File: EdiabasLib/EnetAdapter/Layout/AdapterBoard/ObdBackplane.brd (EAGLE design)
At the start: 36 x 20 mm, 11 parts, among them J1 OBDII, U1 FPC-FFC-CONNECTOR-08-1MM, U2 FPC-FFC-CONNECTOR-08-1MM-L

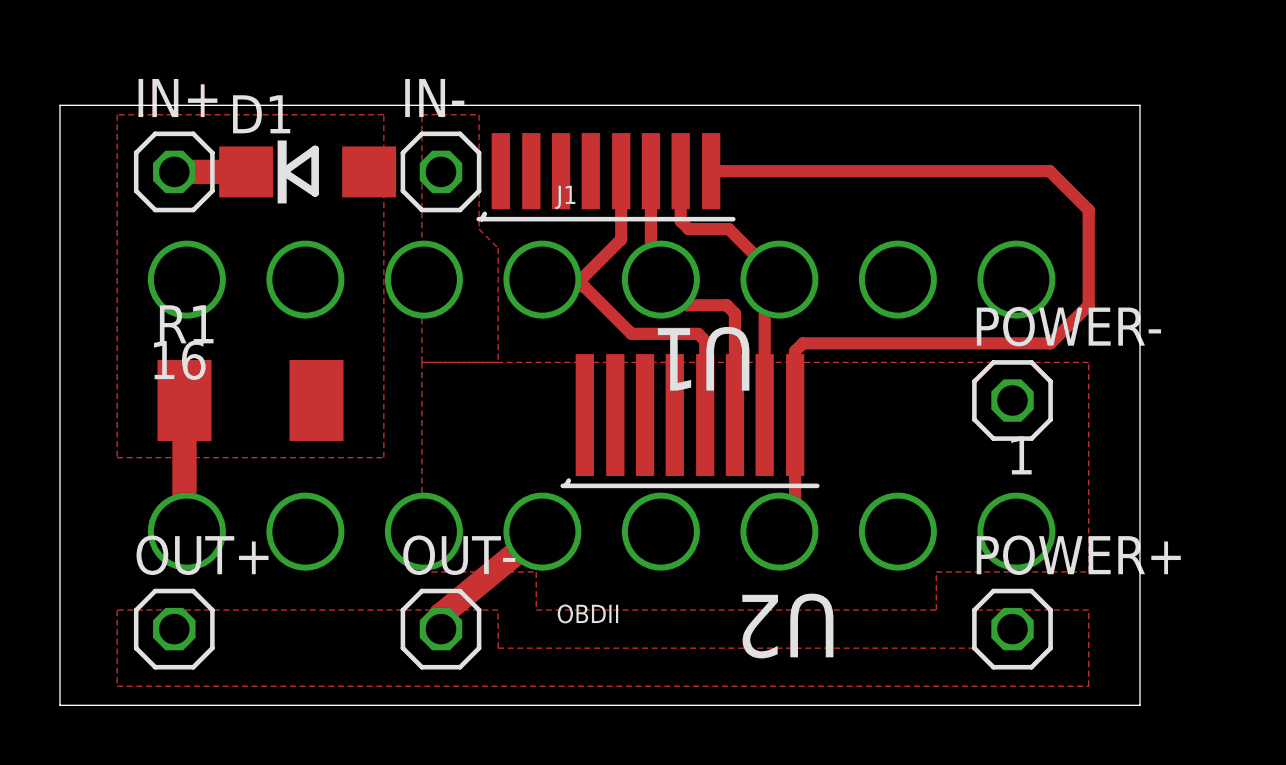
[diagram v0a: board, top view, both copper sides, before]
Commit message: Using larger resistor
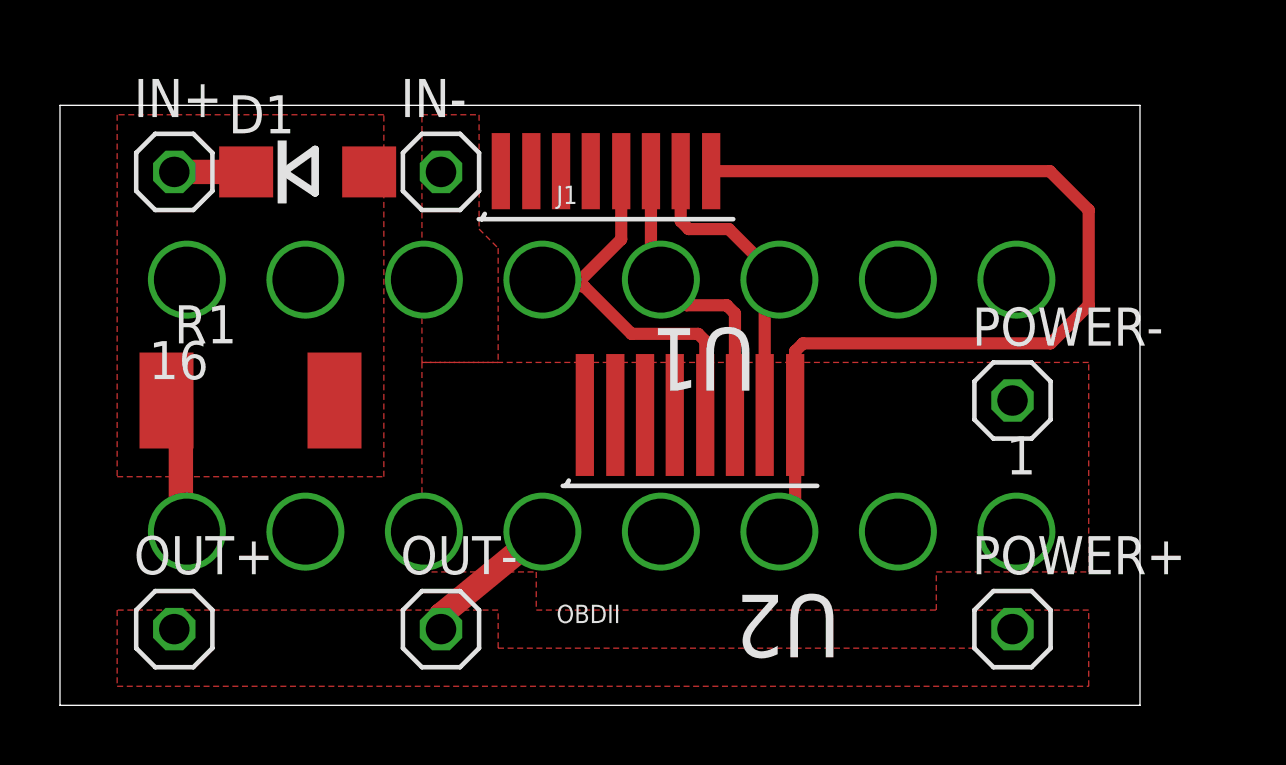
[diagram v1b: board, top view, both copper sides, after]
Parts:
- R1: device rcl:R2010 -> resistor:R2512
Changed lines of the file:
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@@
 <element name="OUT+" library="pinhead" package="1X01" value="5V" x="3.81" y="2.54"/>
 <element name="OUT-" library="pinhead" package="1X01" value="GND" x="12.7" y="2.54"/>
-<element name="R1" library="rcl" package="R2010" value="511" x="6.35" y="10.16"/>
+<element name="R1" library="resistor" package="R2512" value="511" x="6.35" y="10.16"/>
 <element name="POWER+" library="pinhead" package="1X01" value="5V" x="31.75" y="2.54"/>
 <element name="POWER-" library="pinhead" package="1X01" value="GND" x="31.75" y="10.16"/>
@@
 <polygon width="0.254" layer="1" isolate="0.4064">
 <vertex x="1.905" y="19.685"/>
-<vertex x="1.905" y="8.255"/>
-<vertex x="10.795" y="8.255"/>
+<vertex x="1.905" y="7.62"/>
+<vertex x="10.795" y="7.62"/>
 <vertex x="10.795" y="19.685"/>
 </polygon>
@@
 <contactref element="J1" pad="8"/>
 <contactref element="R1" pad="1"/>
-<wire x1="4.15" y1="10.16" x2="4.03" y2="10.16" width="0.8128" layer="1"/>
-<wire x1="4.15" y1="10.16" x2="4.15" y2="5.87" width="0.8128" layer="1"/>
-<wire x1="4.15" y1="5.87" x2="4.23" y2="5.79" width="0.8128" layer="1"/>
+<wire x1="3.55" y1="10.16" x2="4.03" y2="10.16" width="0.8128" layer="1"/>
+<wire x1="4.03" y1="10.16" x2="4.03" y2="5.99" width="0.8128" layer="1"/>
+<wire x1="4.03" y1="5.99" x2="4.23" y2="5.79" width="0.8128" layer="1"/>
 </signal>
 <signal name="N$1">

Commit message: Layout for elecrow
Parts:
- removed U2: FPC-FFC-CONNECTOR-08-1MM-L, obd_special:FPC-FFC-CONNECTOR-08-1MM-L
- U1: value FPC-FFC-CONNECTOR-08-1MM -> FPC-FFC-CONNECTOR-08-1MM-L; device obd_special:FPC-FFC-CONNECTOR-08-1MM -> obd_special:FPC-FFC-CONNECTOR-08-1MM-L
- moved U1 9.02 mm to (20.3, 7.75)
- moved POWER+ 3.81 mm to (27.9, 2.54)
- moved POWER- 3.81 mm to (27.9, 10.2)
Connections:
- net GND: no longer IN-.1
- net N$3: no longer U2.8
- net N$4: no longer U2.7
- net N$5: no longer U2.6
- net N$6: now also U1.3; no longer U1.5, U2.5
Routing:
- net N$3: track 32.9 -> 4.08 mm
- net GND: track 4.85 -> 20.9 mm
- net +12V: track 0.00 -> 7.71 mm
- net N$6: track 13.2 -> 6.02 mm
- net N$4: track 10.5 -> 4.87 mm
- net N$5: track 10.1 -> 5.13 mm
- added copper zone on layer 16, net +5V
- removed copper zone on layer 1, net +5V
- removed copper zone on layer 1, net GND
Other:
- board size 36 x 20 mm -> 33 x 20 mm

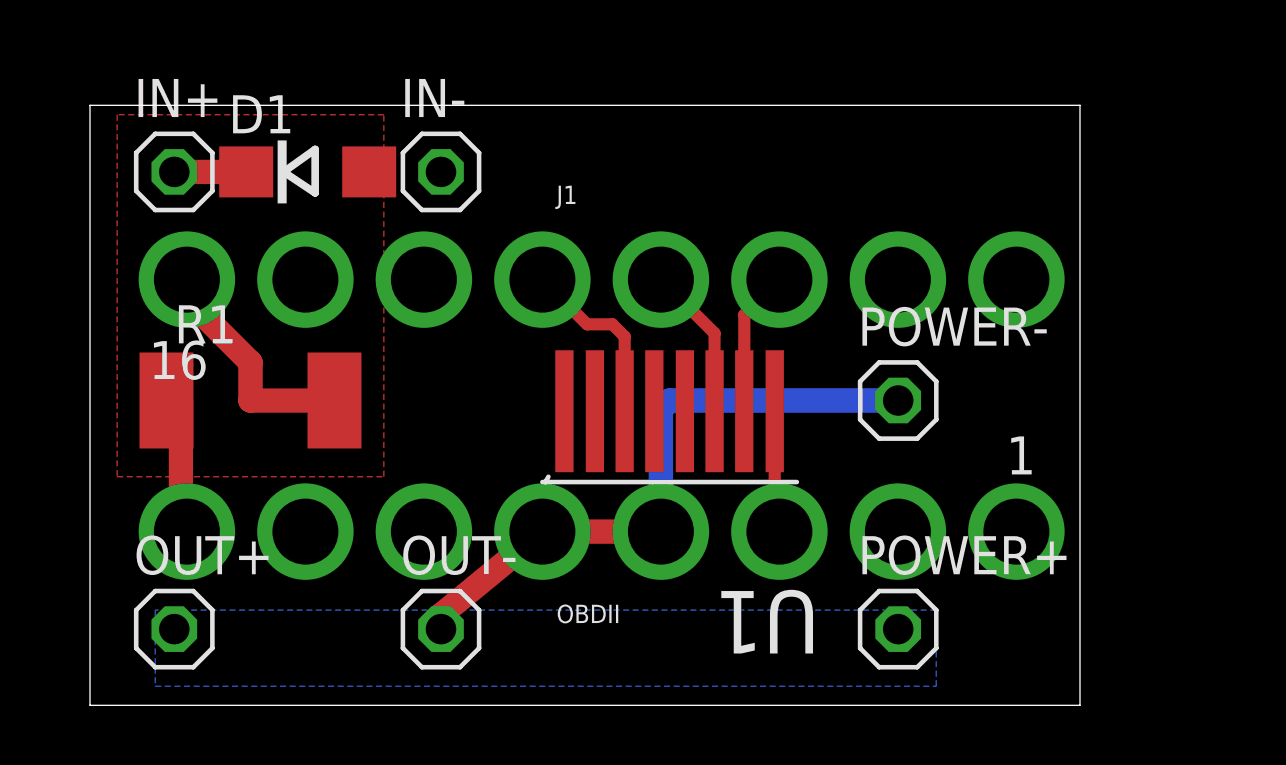
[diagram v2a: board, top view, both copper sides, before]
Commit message: Improved adapter layout
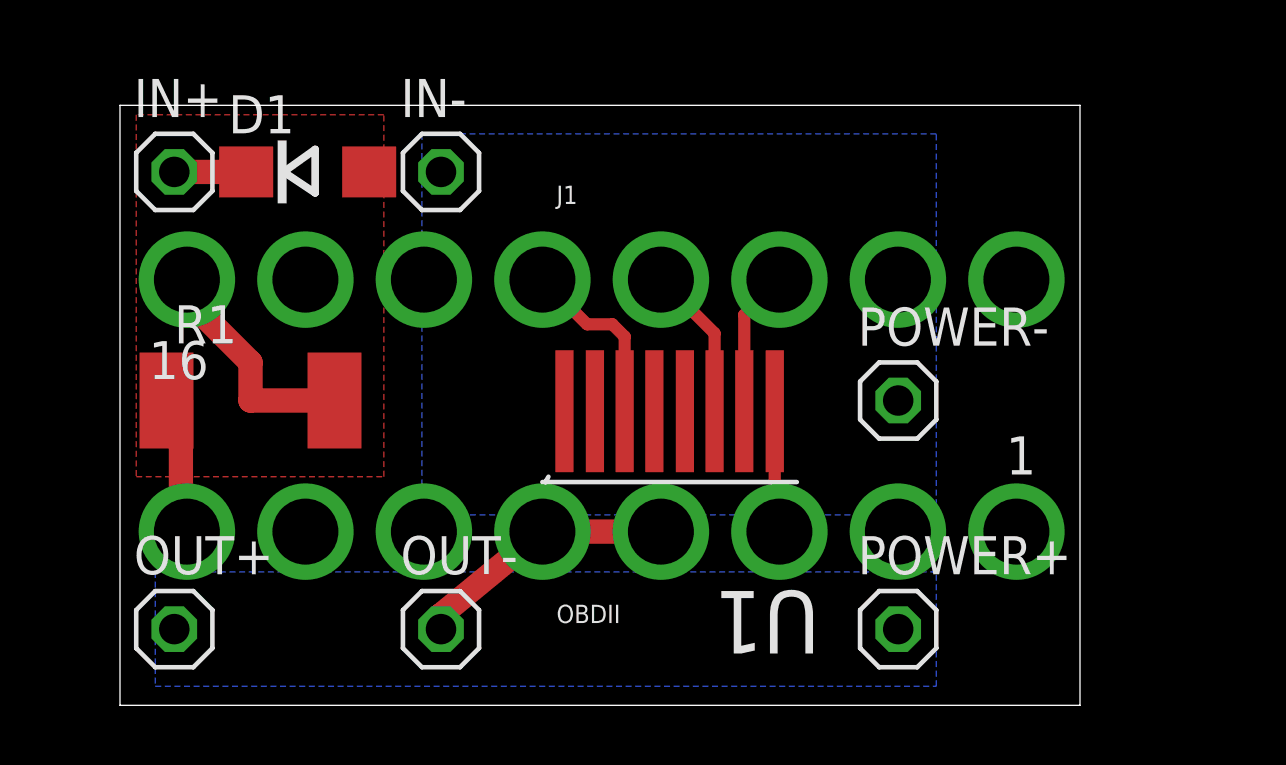
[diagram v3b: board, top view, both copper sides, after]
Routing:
- net GND: track 20.9 -> 8.80 mm
- added copper zone on layer 16, net GND
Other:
- board size 33 x 20 mm -> 32 x 20 mm
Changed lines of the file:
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@@
 <board>
 <plain>
-<wire x1="1" y1="0" x2="34" y2="0" width="0" layer="20"/>
+<wire x1="2" y1="0" x2="34" y2="0" width="0" layer="20"/>
 <wire x1="34" y1="0" x2="34" y2="20" width="0" layer="20"/>
-<wire x1="34" y1="20" x2="1" y2="20" width="0" layer="20"/>
-<wire x1="1" y1="20" x2="1" y2="0" width="0" layer="20"/>
+<wire x1="34" y1="20" x2="2" y2="20" width="0" layer="20"/>
+<wire x1="2" y1="20" x2="2" y2="0" width="0" layer="20"/>
 </plain>
 <attributes>
@@
 <wire x1="12.7" y1="2.54" x2="12.7" y2="3.01" width="0.8128" layer="1"/>
 <wire x1="12.7" y1="3.01" x2="16.08" y2="5.79" width="0.8128" layer="1"/>
-<wire x1="20.03" y1="5.79" x2="20.03" y2="9.87" width="0.8128" layer="16"/>
-<wire x1="20.03" y1="9.87" x2="20.32" y2="10.16" width="0.8128" layer="16"/>
-<wire x1="20.32" y1="10.16" x2="27.94" y2="10.16" width="0.8128" layer="16"/>
 <wire x1="16.08" y1="5.79" x2="20.03" y2="5.79" width="0.8128" layer="1"/>
+<polygon width="0.254" layer="16" spacing="0.254" isolate="0.4064">
+<vertex x="29.21" y="6.35"/>
+<vertex x="29.21" y="19.05"/>
+<vertex x="12.065" y="19.05"/>
+<vertex x="12.065" y="6.35"/>
+</polygon>
 </signal>
 <signal name="+12V">
@@
 <contactref element="D1" pad="A"/>
 <polygon width="0.254" layer="1" isolate="0.4064">
-<vertex x="1.905" y="19.685"/>
-<vertex x="1.905" y="7.62"/>
+<vertex x="2.54" y="19.685"/>
+<vertex x="2.54" y="7.62"/>
 <vertex x="10.795" y="7.62"/>
 <vertex x="10.795" y="19.685"/>
@@
 <vertex x="3.175" y="0.635"/>
 <vertex x="29.21" y="0.635"/>
-<vertex x="29.21" y="3.175"/>
-<vertex x="3.175" y="3.175"/>
+<vertex x="29.21" y="4.445"/>
+<vertex x="3.175" y="4.445"/>
 </polygon>
 </signal>

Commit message: FFC connector replaced
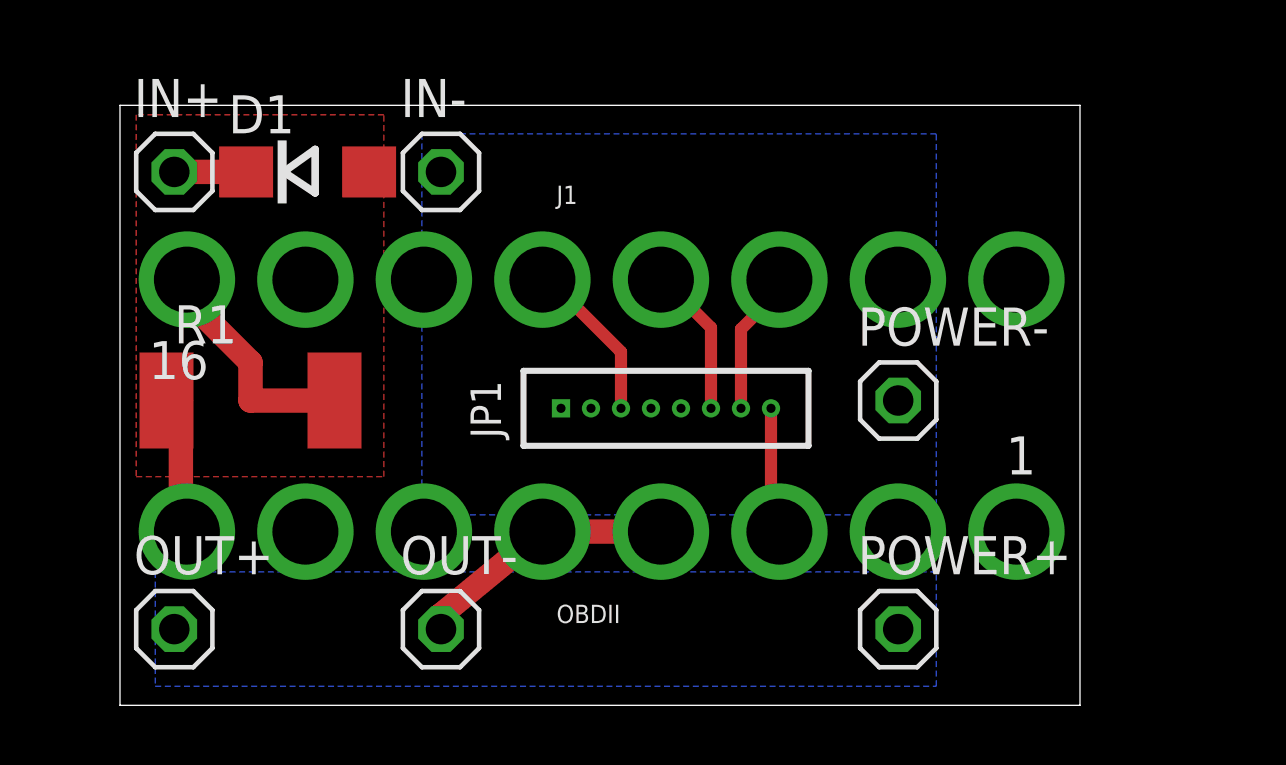
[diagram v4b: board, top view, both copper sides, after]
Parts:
- removed U1: FPC-FFC-CONNECTOR-08-1MM-L, obd_special:FPC-FFC-CONNECTOR-08-1MM-L
- added JP1: (no value), obd_special:1X08M-1MM
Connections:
- removed net N$5: J1.12, U1.6
- new net N$7: J1.11, JP1.7
- net N$3: now also JP1.8; no longer U1.8
- net N$4: now also J1.12, JP1.6; no longer J1.11, U1.7
- net N$6: now also JP1.3; no longer U1.3
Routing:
- net N$5: track 5.13 -> 0.00 mm
- net N$7: track 0.00 -> 4.82 mm
- net N$6: track 6.02 -> 5.50 mm
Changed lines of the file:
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@@
 <element name="POWER+" library="pinhead" package="1X01" value="5V" x="27.94" y="2.54"/>
 <element name="POWER-" library="pinhead" package="1X01" value="GND" x="27.94" y="10.16"/>
-<element name="U1" library="obd_special" package="FPC-FFC-CONNECTOR-08-1MM-L" value="FPC-FFC-CONNECTOR-08-1MM-L" x="20.32" y="7.747" rot="R180"/>
+<element name="JP1" library="obd_special" package="1X08M-1MM" value="" x="20.2" y="9.9"/>
 </elements>
 <signals>
@@
 <signal name="N$3">
 <contactref element="J1" pad="3"/>
-<contactref element="U1" pad="8"/>
-<wire x1="23.8252" y1="9.8044" x2="23.8252" y2="5.9448" width="0.4064" layer="1"/>
-<wire x1="23.8252" y1="5.9448" x2="23.98" y2="5.79" width="0.4064" layer="1"/>
-</signal>
-<signal name="N$4">
-<contactref element="J1" pad="11"/>
-<contactref element="U1" pad="7"/>
-<wire x1="22.8092" y1="9.8044" x2="22.8092" y2="13.0192" width="0.4064" layer="1"/>
-<wire x1="22.8092" y1="13.0192" x2="23.98" y2="14.19" width="0.4064" layer="1"/>
-</signal>
-<signal name="N$5">
-<contactref element="J1" pad="12"/>
-<contactref element="U1" pad="6"/>
-<wire x1="21.8186" y1="9.8044" x2="21.8186" y2="12.4014" width="0.4064" layer="1"/>
-<wire x1="21.8186" y1="12.4014" x2="20.03" y2="14.19" width="0.4064" layer="1"/>
+<contactref element="JP1" pad="8"/>
+<wire x1="23.7" y1="9.9" x2="23.7" y2="6.07" width="0.4064" layer="1"/>
+<wire x1="23.7" y1="6.07" x2="23.98" y2="5.79" width="0.4064" layer="1"/>
 </signal>
 <signal name="N$6">
 <contactref element="J1" pad="13"/>
-<contactref element="U1" pad="3"/>
-<wire x1="18.8214" y1="9.8044" x2="18.8214" y2="12.2936" width="0.4064" layer="1"/>
-<wire x1="18.8214" y1="12.2936" x2="18.415" y2="12.7" width="0.4064" layer="1"/>
-<wire x1="18.415" y1="12.7" x2="17.57" y2="12.7" width="0.4064" layer="1"/>
-<wire x1="17.57" y1="12.7" x2="16.08" y2="14.19" width="0.4064" layer="1"/>
+<contactref element="JP1" pad="3"/>
+<wire x1="18.7" y1="9.9" x2="18.7" y2="11.78" width="0.4064" layer="1"/>
+<wire x1="18.7" y1="11.78" x2="16.51" y2="13.97" width="0.4064" layer="1"/>
+<wire x1="16.51" y1="13.97" x2="16.3" y2="13.97" width="0.4064" layer="1"/>
+<wire x1="16.3" y1="13.97" x2="16.08" y2="14.19" width="0.4064" layer="1"/>
+</signal>
+<signal name="N$7">
+<contactref element="J1" pad="11"/>
+<contactref element="JP1" pad="7"/>
+<wire x1="22.7" y1="9.9" x2="22.7" y2="12.54" width="0.4064" layer="1"/>
+<wire x1="22.7" y1="12.54" x2="23.495" y2="13.335" width="0.4064" layer="1"/>
+<wire x1="23.495" y1="13.335" x2="23.495" y2="13.705" width="0.4064" layer="1"/>
+<wire x1="23.495" y1="13.705" x2="23.98" y2="14.19" width="0.4064" layer="1"/>
+</signal>
+<signal name="N$4">
+<contactref element="J1" pad="12"/>
+<contactref element="JP1" pad="6"/>
+<wire x1="21.7" y1="9.9" x2="21.7" y2="12.59" width="0.4064" layer="1"/>
+<wire x1="21.7" y1="12.59" x2="20.32" y2="13.97" width="0.4064" layer="1"/>
+<wire x1="20.32" y1="13.97" x2="20.25" y2="13.97" width="0.4064" layer="1"/>
+<wire x1="20.25" y1="13.97" x2="20.03" y2="14.19" width="0.4064" layer="1"/>
 </signal>
 </signals>

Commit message: Connector layout improved
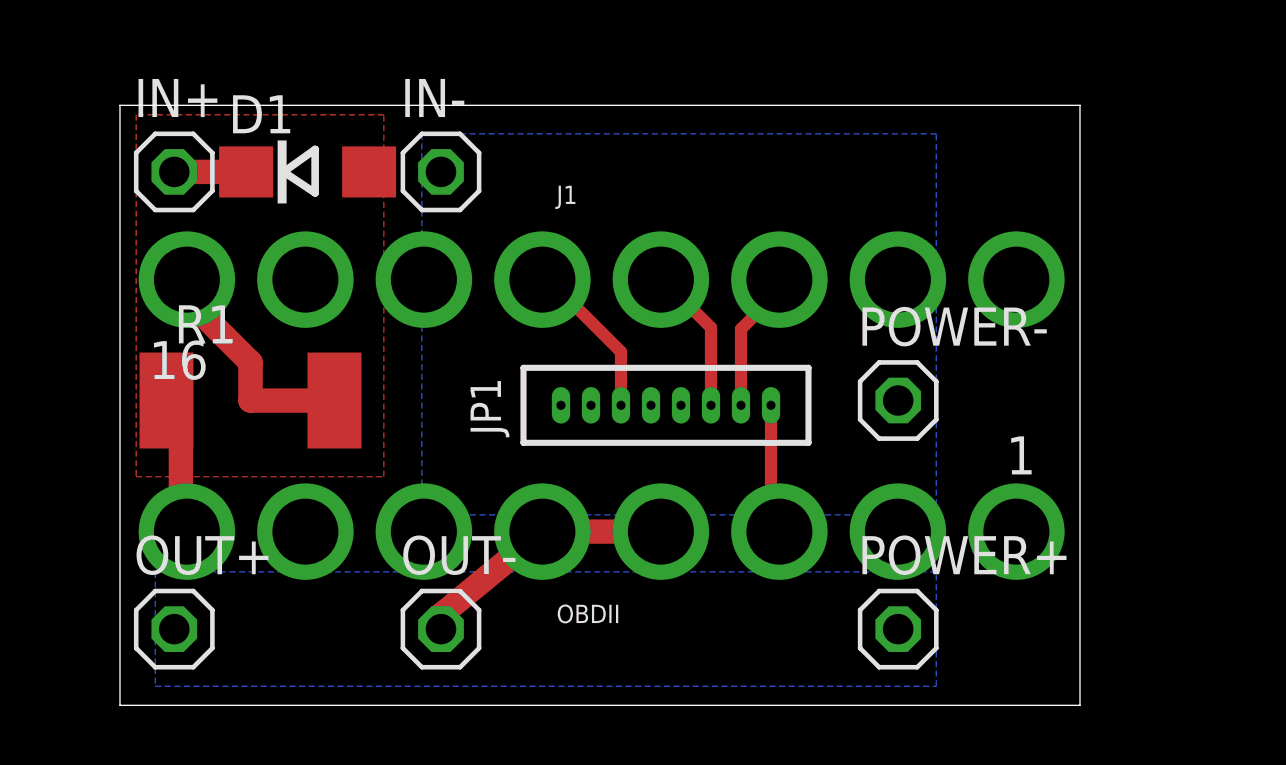
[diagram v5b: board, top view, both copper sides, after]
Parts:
- JP1: value (none) -> ETHERNET
- moved JP1 0.10 mm to (20.2, 10.0)
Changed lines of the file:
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@@
 <element name="POWER+" library="pinhead" package="1X01" value="5V" x="27.94" y="2.54"/>
 <element name="POWER-" library="pinhead" package="1X01" value="GND" x="27.94" y="10.16"/>
-<element name="JP1" library="obd_special" package="1X08M-1MM" value="" x="20.2" y="9.9"/>
+<element name="JP1" library="obd_special" package="1X08M-1MM" value="ETHERNET" x="20.2" y="10"/>
 </elements>
 <signals>
@@
 <contactref element="J1" pad="3"/>
 <contactref element="JP1" pad="8"/>
-<wire x1="23.7" y1="9.9" x2="23.7" y2="6.07" width="0.4064" layer="1"/>
+<wire x1="23.7" y1="10" x2="23.7" y2="6.07" width="0.4064" layer="1"/>
 <wire x1="23.7" y1="6.07" x2="23.98" y2="5.79" width="0.4064" layer="1"/>
 </signal>
@@
 <contactref element="J1" pad="13"/>
 <contactref element="JP1" pad="3"/>
-<wire x1="18.7" y1="9.9" x2="18.7" y2="11.78" width="0.4064" layer="1"/>
+<wire x1="18.7" y1="10" x2="18.7" y2="11.78" width="0.4064" layer="1"/>
 <wire x1="18.7" y1="11.78" x2="16.51" y2="13.97" width="0.4064" layer="1"/>
 <wire x1="16.51" y1="13.97" x2="16.3" y2="13.97" width="0.4064" layer="1"/>
@@
 <contactref element="J1" pad="11"/>
 <contactref element="JP1" pad="7"/>
-<wire x1="22.7" y1="9.9" x2="22.7" y2="12.54" width="0.4064" layer="1"/>
+<wire x1="22.7" y1="10" x2="22.7" y2="12.54" width="0.4064" layer="1"/>
 <wire x1="22.7" y1="12.54" x2="23.495" y2="13.335" width="0.4064" layer="1"/>
 <wire x1="23.495" y1="13.335" x2="23.495" y2="13.705" width="0.4064" layer="1"/>
@@
 <contactref element="J1" pad="12"/>
 <contactref element="JP1" pad="6"/>
-<wire x1="21.7" y1="9.9" x2="21.7" y2="12.59" width="0.4064" layer="1"/>
+<wire x1="21.7" y1="10" x2="21.7" y2="12.59" width="0.4064" layer="1"/>
 <wire x1="21.7" y1="12.59" x2="20.32" y2="13.97" width="0.4064" layer="1"/>
 <wire x1="20.32" y1="13.97" x2="20.25" y2="13.97" width="0.4064" layer="1"/>

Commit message: Layout improved
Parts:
- removed POWER+: 5V, pinhead:1X01
- removed POWER-: GND, pinhead:1X01
- added P+: 5V, pinhead:1X01
- added P-: GND, pinhead:1X01
- renumbered J1 to OBDII
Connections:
- net +5V: now also P+.1; no longer POWER+.1
- net GND: now also P-.1; no longer POWER-.1
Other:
- board size 32 x 20 mm -> 32 x 19.5 mm
